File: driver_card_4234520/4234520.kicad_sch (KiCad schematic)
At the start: 30 parts, among them U1 74LS74, U10 74LS155, U11 74LS02, U12 74LS09, U13 74LS244, U14 74LS244, U15 74LS21, U16 74LS244, U17 74LS374, U18 74LS374, U19 74LS374, U2 74LS08, U20 74LS245, U21 74LS244, U22 74LS244, U23 74LS244, U24 74LS32, U3 74LS04, U4 74LS74, U5 74LS32, U6 74LS10, U7 74LS74, U8 74LS138, U9 74LS00

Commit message: Tracing finished
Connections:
- net ##4: no longer U2.4
- net ##5: now also U7.11 (C); no longer U2.11
- net 5V: now also U7.10 (~{S}), U7.12 (D)
- net GND: now also U13.1 (OEa), U16.1 (OEa), U21.1 (OEa), U21.19 (OEb), U22.1 (OEa), U22.19 (OEb), U23.1 (OEa), U23.19 (OEb)
- net ##28: now reaches U1.2 (D)
- net ##28: now also J?.51, R3.13, U14.18 (O0a), U17.2 (O0), U17.3 (D0), U18.2 (O0), U19.2 (O0), U20.2 (A0)
- net ##29: now reaches U1.3 (C)
- net ##29: now also U10.12 (Q3b)
- net ##30: now reaches U1.5 (Q)
- net ##30: now also U14.2 (I0a), U4.4 (~{S})
- net ##31: now reaches U1.6 (~{Q})
- net ##31: now also U11.3, U13.19 (OEb), U16.19 (OEb), U16.6 (I2a), U24.10, U24.2, U24.5
- net ##44: now reaches U7.13 (~{R})
- net ##44: now also U10.10 (Q1b)
- net ##46: now reaches U7.9 (Q)
- net ##46: now also U14.4 (I1a)
- net ##32: now reaches U2.2
- net ##32: now also U4.6 (~{Q})
- net ##35: now reaches U2.5
- net ##35: now also J?.3, R1.10
- net ##36: now reaches U3.2
- net ##36: now also U10.1 (Ea1)
- net ##37: now reaches U3.3
- net ##37: now also J?.2 (RESET), U24.12
- net ##50: now reaches R1.11
- net ##50: now also J?.43, U24.1
- net ##60: now reaches R1.2
- net ##60: now also J?.45, U14.17 (I3b), U16.13 (I1b)
- net ##61: now reaches R1.4
- net ##61: now also J?.49, U14.15 (I2b), U24.9
- net ##62: now reaches R1.6
- net ##62: now also J?.25, U14.11 (I0b), U24.4
- net ##51: now reaches R1.9
- net ##51: now also J?.4, U11.2, U14.6 (I2a)
- net ##38: now reaches U3.6
- net ##38: now also U5.5, U6.1
- net ##64: now reaches U10.13 (A0)
- net ##64: now also J?.13, U19.7 (D2), U22.16 (O1a)
- net ##63: now reaches U10.14 (Eb1)
- net ##63: now also U13.12 (O3a)
- net ##23: now reaches U10.15 (Eb2)
- net ##23: now also U10.2 (Ea2), U5.9, U8.10 (O5)
- net ##76: now reaches U10.3 (A1)
- net ##76: now also J?.12, U19.8 (D3), U22.5 (O2b)
- net ##77: now reaches U10.4 (Q3a)
- net ##77: now also U14.1 (OEa), U14.19 (OEb)
- net ##78: now reaches U10.5 (Q2a)
- net ##78: now also U18.1 (OE)
- net ##79: now reaches U10.6 (Q1a)
- net ##79: now also U19.1 (OE)
- net ##80: now reaches U10.7 (Q0a)
- net ##80: now also U17.1 (OE)
- net ##65: now reaches U10.9 (Q0b)
- net ##65: now also U17.11 (Cp)
- net ##43: now reaches U11.1
- net ##43: now also U6.2
- net ##39: now reaches U4.3 (C)
- net ##39: now also U16.18 (O0a)
- net ##81: now reaches U11.5
- net ##81: now also J?.15, U18.4 (D1), U21.14 (O2a)
- net ##82: now reaches U11.6
- net ##82: now also J?.41, U18.7 (D2), U21.16 (O1a)
- net ##40: now reaches U5.1
- net ##40: now also J?.29, U11.12, U23.9 (O0b), U8.5 (E2)
- net ##41: now reaches U5.3
- net ##41: now also U9.9
- net ##67: now reaches U11.8
- net ##67: now also J?.9, U18.14 (D5), U21.5 (O2b)
- net ##66: now reaches U11.9
- net ##66: now also J?.38, U18.17 (D6), U21.7 (O1b)
- net ##25: now reaches U5.4
- net ##25: now also U6.13, U9.8
- net ##42: now reaches U5.6
- net ##42: now also U6.4, U6.5
- net ##48: now reaches U11.11
- net ##48: now also U13.18 (O0a), U9.12
- net ##57: now reaches U11.13
- net ##57: now also U9.4
- net ##24: now reaches U5.8
- net ##24: now also U6.11
- net ##83: now reaches U12.2
- net ##83: now also R2.1, U16.7 (O1b)
- net ##84: now reaches U12.3
- net ##84: now also J?.41 (IO_READY), R2.5
- net ##85: now reaches U12.4
- net ##85: now also U12.5, U24.3
- net ##86: now reaches U12.6
- net ##86: now also J?.21 (IRQ7), R2.2
- net ##70: now reaches U12.10
- net ##70: now also U12.9, U24.6
- net ##71: now reaches U12.8
- net ##71: now also J?.8 (UNUSED), R2.13
- net ##26: now reaches U6.12
- net ##26: now also U6.3
- net ##69: now reaches U12.11
- net ##69: now also J?.32 (IO), R2.4
- net ##68: now reaches U12.12
- net ##68: now also U12.13, U24.8
- net ##27: now reaches U6.8
- net ##27: now also U20.1 (A->B)
- net ##75: now reaches U13.11 (I0b)
- net ##75: now also J?.11 (~{SMEMW}), U13.2 (I0a)
- net ##74: now reaches U13.13 (I1b)
- net ##74: now also J?.14 (~{IOR}), U13.4 (I1a)
- net ##47: now reaches U13.14 (O2a)
- net ##47: now also U9.10, U9.13
- net ##73: now reaches U13.15 (I2b)
- net ##73: now also J?.12 (~{SMEMR}), U13.6 (I2a)
- net ##72: now reaches U13.17 (I3b)
- net ##72: now also J?.13 (~{IOW}), U13.8 (I3a)
- net ##87: now reaches U13.3 (O3b)
- net ##87: now also J?.20, R2.12
- net ##88: now reaches U13.5 (O2b)
- net ##88: now also J?.34, R2.10
- net ##89: now reaches U13.7 (O1b)
- net ##89: now also J?.39, R2.9
- net ##90: now reaches U13.9 (O0b)
- net ##90: now also J?.35, R2.8
- net ##52: now reaches U8.1 (A0)
- net ##52: now also J?.21, U19.14 (D5), U22.7 (O1b)
- net ##53: now reaches U8.2 (A1)
- net ##53: now also J?.32, U19.13 (D4), U22.14 (O2a)
- net ##54: now reaches U8.4 (E1)
- net ##54: now also U9.3
- net ##45: now reaches U8.6 (E3)
- net ##45: now also U2.11
- net ##55: now reaches U9.1
- net ##55: now also J?.31, U19.17 (D6), U22.12 (O3a)
- net ##56: now reaches U9.2
- net ##56: now also J?.11, U19.18 (D7), U22.9 (O0b)
- net ##93: now reaches U14.12 (O3a)
- net ##93: now also J?.56, R3.10, U17.8 (D3), U17.9 (O3), U18.9 (O3), U19.9 (O3), U20.5 (A3)
- net ##92: now reaches U14.14 (O2a)
- net ##92: now also J?.52, R3.11, U17.6 (O2), U17.7 (D2), U18.6 (O2), U19.6 (O2), U20.4 (A2)
- net ##91: now reaches U14.16 (O1a)
- net ##91: now also J?.48, R3.12, U17.4 (D1), U17.5 (O1), U18.5 (O1), U19.5 (O1), U20.3 (A1)
- net ##101: now reaches U14.3 (O3b)
- net ##101: now also J?.47, R2.3, U17.18 (D7), U17.19 (O7), U18.19 (O7), U19.19 (O7), U20.9 (A7)
- net ##102: now reaches U14.5 (O2b)
- net ##102: now also J?.44, R2.6, U17.16 (O6), U17.17 (D6), U18.16 (O6), U19.16 (O6), U20.8 (A6)
- net ##103: now reaches U14.7 (O1b)
- net ##103: now also J?.22, R2.7, U17.14 (D5), U17.15 (O5), U18.15 (O5), U19.15 (O5), U20.7 (A5)
- net ##98: now reaches U14.8 (I3a)
- net ##98: now also J?.1, R2.11
- net ##104: now reaches U14.9 (O0b)
- net ##104: now also J?.53, R3.9, U17.12 (O4), U17.13 (D4), U18.12 (O4), U19.12 (O4), U20.6 (A4)
- net ##105: now reaches U15.1
- net ##105: now also J?.30, U23.12 (O3a)
- net ##106: now reaches U15.2
- net ##106: now also J?.33, U23.14 (O2a)
- net ##107: now reaches U15.4
- net ##107: now also J?.7, U23.16 (O1a)
- net ##108: now reaches U15.5
- net ##108: now also J?.8, U23.18 (O0a)
- net ##58: now reaches U15.6
- net ##58: now also U9.5
- net ##96: now reaches U15.10
- net ##96: now also J?.16, U18.8 (D3), U21.18 (O0a)
- net ##95: now reaches U15.12
- net ##95: now also J?.18, U18.13 (D4), U21.3 (O3b)
- net ##94: now reaches U15.13
- net ##94: now also J?.14, U19.4 (D1), U22.3 (O3b)
- net ##97: now reaches U15.9
- net ##97: now also J?.36, U18.3 (D0), U21.12 (O3a)
- net ##59: now reaches U9.6
- net ##59: now also U18.11 (Cp), U19.11 (Cp)
- net ##49: now reaches U9.11
- net ##49: now also U2.4
- net ##100: now reaches U16.12 (O3a)
- net ##100: now also J?.10
- net ##99: now reaches U16.14 (O2a)
- net ##99: now also J?.28
- net ##141: now reaches U16.2 (I0a)
- net ##141: now also J?.20 (CLK)
- net ##109: now reaches U16.4 (I1a)
- net ##109: now also J?.2, ZR1.6 (R3.2)
- net ##117: now reaches U20.11 (B7)
- net ##117: now also J?.33 (DB7), R3.8
- net ##116: now reaches U20.12 (B6)
- net ##116: now also J?.34 (DB6), R3.7
- net ##115: now reaches U20.13 (B5)
- net ##115: now also J?.35 (DB5), R3.6
- net ##114: now reaches U20.14 (B4)
- net ##114: now also J?.36 (DB4), R3.5
- net ##113: now reaches U20.15 (B3)
- net ##113: now also J?.37 (DB3), R3.4
- net ##112: now reaches U20.16 (B2)
- net ##112: now also J?.38 (DB2), R3.3
- net ##111: now reaches U20.17 (B1)
- net ##111: now also J?.39 (DB1), R3.2
- net ##110: now reaches U20.18 (B0)
- net ##110: now also J?.40 (DB0), R3.1
- net ##121: now reaches U21.11 (I0b)
- net ##121: now also J?.55 (BA07)
- net ##120: now reaches U21.13 (I1b)
- net ##120: now also J?.56 (BA06)
- net ##119: now reaches U21.15 (I2b)
- net ##119: now also J?.57 (BA05)
- net ##118: now reaches U21.17 (I3b)
- net ##118: now also J?.58 (BA04)
- net ##125: now reaches U21.2 (I0a)
- net ##125: now also J?.59 (BA03)
- net ##124: now reaches U21.4 (I1a)
- net ##124: now also J?.60 (BA02)
- net ##123: now reaches U21.6 (I2a)
- net ##123: now also J?.61 (BA01)
- net ##122: now reaches U21.8 (I3a)
- net ##122: now also J?.62 (BA00)
- net ##129: now reaches U22.11 (I0b)
- net ##129: now also J?.47 (BA15)
- net ##128: now reaches U22.13 (I1b)
- net ##128: now also J?.49 (BA13)
- net ##127: now reaches U22.15 (I2b)
- net ##127: now also J?.51 (BA11)
- net ##126: now reaches U22.17 (I3b)
- net ##126: now also J?.53 (BA09)
- net ##133: now reaches U22.2 (I0a)
- net ##133: now also J?.54 (BA08)
- net ##132: now reaches U22.4 (I1a)
- net ##132: now also J?.52 (BA10)
- net ##131: now reaches U22.6 (I2a)
- net ##131: now also J?.50 (BA12)
- net ##130: now reaches U22.8 (I3a)
- net ##130: now also J?.48 (BA14)
- net ##135: now reaches U23.11 (I0b)
- net ##135: now also J?.42 (AEN)
- net ##134: now reaches U23.13 (I1b)
- net ##134: now also J?.28 (ALE)
- net ##139: now reaches U23.2 (I0a)
- net ##139: now also J?.46 (BA16)
- net ##138: now reaches U23.4 (I1a)
- net ##138: now also J?.45 (BA17)
- net ##137: now reaches U23.6 (I2a)
- net ##137: now also J?.44 (BA18)
- net ##140: now reaches U23.7 (O1b)
- net ##140: now also J?.26
- net ##136: now reaches U23.8 (I3a)
- net ##136: now also J?.43 (BA19)
- no-connect marks 0 -> 54

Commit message: copy over PCB layout from earlier project add custom symbols for r networks add custom footprint for ISA XT bus add and label test point vias add filter caps missing from original schematic
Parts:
- added C1, C2, C4, C5, C6, C7, C8: 104, Capacitor_THT:C_Rect_L7.0mm_W2.0mm_P5.00mm, symbol Device:C
- added C3, C9: 106, Capacitor_THT:C_Rect_L7.0mm_W2.0mm_P5.00mm, symbol Device:C_Polarized_Small_US
- J1: renamed from J?; footprint (none) -> custom:BUS_XT
- J2: renamed from J?; footprint (none) -> Connector_Dsub:DSUB-62-HD_Female_Horizontal_P2.41x1.98mm_EdgePinOffset3.03mm_Housed_MountingHolesOffset4.94mm
- R1: footprint (none) -> Package_DIP:DIP-16_W7.62mm; symbol custom:316E221331 -> custom:R_Network_Dividers_AB_316E
- R2, R3: footprint (none) -> Package_DIP:DIP-14_W7.62mm; symbol custom:314A822 -> custom:R_Array_AB_314A
- U1, U11, U12, U15, U2, U24, U3, U4, U5, U6, U7, U9: footprint (none) -> Package_DIP:DIP-14_W7.62mm
- U10, U8: footprint (none) -> Package_DIP:DIP-16_W7.62mm
- U13, U14, U16, U17, U18, U19, U20, U21, U22, U23: footprint (none) -> Package_DIP:DIP-20_W7.62mm
- ZR1: symbol Device:R_Pack03_SIP -> custom:R_Array_AB_106B
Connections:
- net 5V: now also C1.1, C2.1, C3.1, C4.1, C5.1, C6.1, C7.1, C8.1, C9.1
- net GND: now also C1.2, C2.2, C3.2, C4.2, C5.2, C6.2, C7.2, C8.2, C9.2

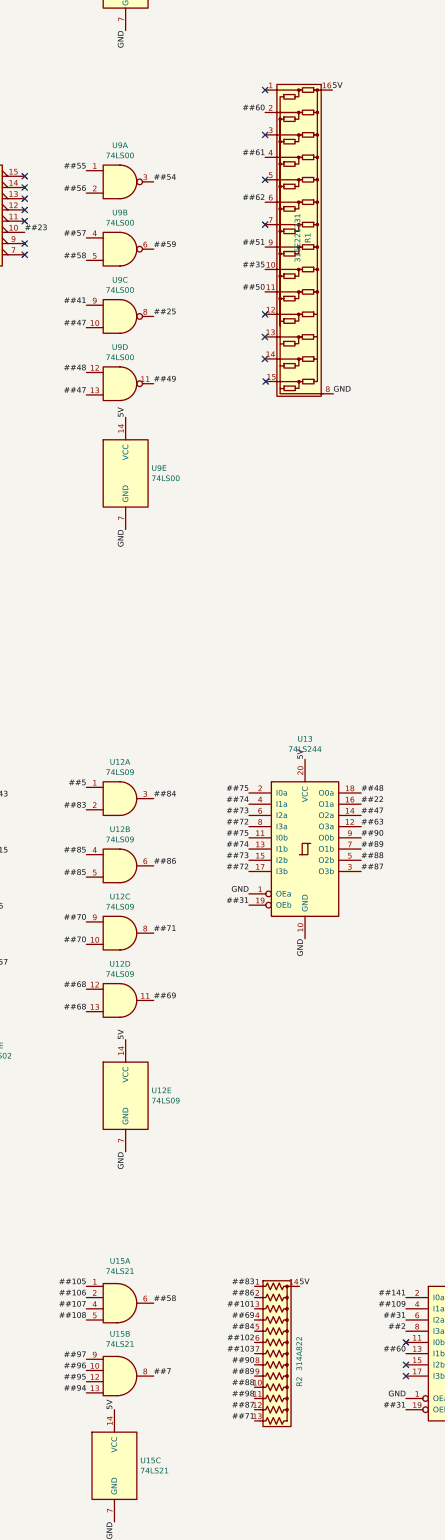
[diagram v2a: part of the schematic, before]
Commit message: make library paths relative convert to 4 layer pcb add gnd and 5v planes symbol cleanup ERC zero errors!
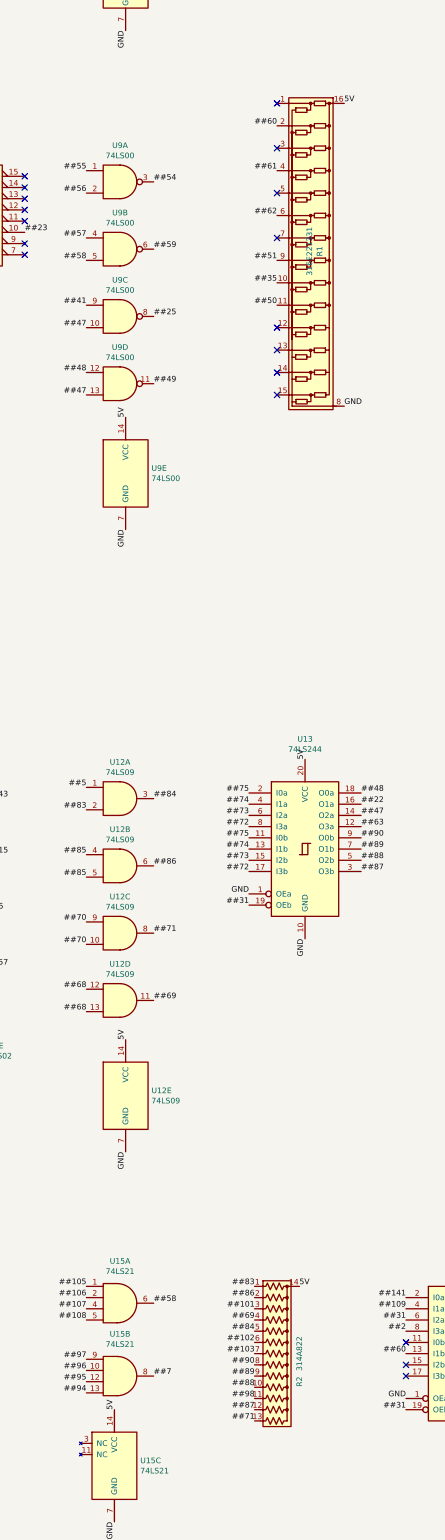
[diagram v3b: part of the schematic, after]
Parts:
- U15: symbol 74xx:74LS21 -> custom:74LS21
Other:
- moved on the sheet: R1
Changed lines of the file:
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@@
 (kicad_sch (version 20230121) (generator eeschema)
   (paper "User" 594.004 840.003)
+  (no_connect (at 153.67 151.13))
   (no_connect (at 109.22 576.58))
   (no_connect (at 96.52 170.18))
   (no_connect (at 72.39 427.99))
   (no_connect (at 297.18 670.56))
-  (no_connect (at 150.9776 158.2674))
+  (no_connect (at 153.67 161.29))
   (no_connect (at 109.22 579.12))
   (no_connect (at 35.56 167.64))
@@
   (no_connect (at 182.88 439.42))
   (no_connect (at 96.52 185.42))
-  (no_connect (at 150.9268 204.0382))
-  (no_connect (at 150.9776 178.5874))
+  (no_connect (at 153.67 207.01))
+  (no_connect (at 153.67 181.61))
   (no_connect (at 96.52 175.26))
   (no_connect (at 35.56 170.18))
-  (no_connect (at 150.9776 198.9074))
+  (no_connect (at 153.67 201.93))
   (no_connect (at 271.78 670.56))
   (no_connect (at 50.8 167.64))
   (no_connect (at 72.39 420.37))
-  (no_connect (at 150.9268 209.0166))
+  (no_connect (at 153.67 212.09))
   (no_connect (at 208.28 436.88))
   (no_connect (at 72.39 422.91))
@@
   (no_connect (at 96.52 177.8))
   (no_connect (at 317.5 670.56))
-  (no_connect (at 151.13 214.122))
+  (no_connect (at 153.67 217.17))
   (no_connect (at 43.18 177.8))
   (no_connect (at 50.8 172.72))
@@
   (no_connect (at 165.1 40.64))
   (no_connect (at 96.52 182.88))
-  (no_connect (at 150.9776 148.1074))
   (no_connect (at 294.64 670.56))
   (no_connect (at 182.88 436.88))
@@
   (no_connect (at 266.7 670.56))
   (no_connect (at 58.42 325.12))
-  (no_connect (at 150.9776 168.4274))
+  (no_connect (at 153.67 171.45))
   (no_connect (at 182.88 431.8))
   (label "##135" (at 307.34 706.12 270) (fields_autoplaced)
@@
     (effects (font (size 1.27 1.27)) (justify left bottom))
   )
-  (label "5V" (at 166.2176 148.1074 0) (fields_autoplaced)
+  (label "5V" (at 168.91 151.13 0) (fields_autoplaced)
     (effects (font (size 1.27 1.27)) (justify left bottom))
   )
@@
     (effects (font (size 1.27 1.27)) (justify right bottom))
   )
-  (label "##51" (at 150.9776 183.6674 180) (fields_autoplaced)
+  (label "##51" (at 153.67 186.69 180) (fields_autoplaced)
     (effects (font (size 1.27 1.27)) (justify right bottom))
   )
@@
     (effects (font (size 1.27 1.27)) (justify right bottom))
   )
-  (label "GND" (at 166.4462 216.916 0) (fields_autoplaced)
+  (label "GND" (at 168.91 219.71 0) (fields_autoplaced)
     (effects (font (size 1.27 1.27)) (justify left bottom))
   )
@@
     (effects (font (size 1.27 1.27)) (justify right bottom))
   )
-  (label "##60" (at 150.9776 153.1874 180) (fields_autoplaced)
+  (label "##60" (at 153.67 156.21 180) (fields_autoplaced)
     (effects (font (size 1.27 1.27)) (justify right bottom))
   )
@@
     (effects (font (size 1.27 1.27)) (justify right bottom))
   )
-  (label "##50" (at 150.9776 193.8274 180) (fields_autoplaced)
+  (label "##50" (at 153.67 196.85 180) (fields_autoplaced)
     (effects (font (size 1.27 1.27)) (justify right bottom))
   )
@@
     (effects (font (size 1.27 1.27)) (justify left bottom))
   )
-  (label "##62" (at 150.9776 173.5074 180) (fields_autoplaced)
+  (label "##62" (at 153.67 176.53 180) (fields_autoplaced)
     (effects (font (size 1.27 1.27)) (justify right bottom))
   )
@@
     (effects (font (size 1.27 1.27)) (justify right bottom))
   )
-  (label "##35" (at 150.9776 188.7474 180) (fields_autoplaced)
+  (label "##35" (at 153.67 191.77 180) (fields_autoplaced)
     (effects (font (size 1.27 1.27)) (justify right bottom))
   )
@@
     (effects (font (size 1.27 1.27)) (justify right bottom))
   )
-  (label "##61" (at 150.9776 163.3474 180) (fields_autoplaced)
+  (label "##61" (at 153.67 166.37 180) (fields_autoplaced)
     (effects (font (size 1.27 1.27)) (justify right bottom))
   )
@@
   (symbol (lib_id "custom:R_Network_Dividers_AB_316E") (at 158.75 181.61 270) (unit 1)
     (in_bom yes) (on_board yes) (dnp no)
-    (property "Reference" "R1" (at 160.655 181.61 0)
+    (property "Reference" "R1" (at 163.3474 184.6326 0)
       (effects (font (size 1.27 1.27)))
     )
-    (property "Value" "316E221331" (at 158.3436 181.61 0)
+    (property "Value" "316E221331" (at 161.036 184.6326 0)
       (effects (font (size 1.27 1.27)))
     )
-    (property "Footprint" "Package_DIP:DIP-16_W7.62mm" (at 158.7246 222.1484 90)
+    (property "Footprint" "Package_DIP:DIP-16_W7.62mm" (at 161.417 225.171 90)
       (effects (font (size 1.27 1.27)) hide)
     )
-    (property "Datasheet" "" (at 158.5976 173.5074 0)
+    (property "Datasheet" "" (at 161.29 176.53 0)
       (effects (font (size 1.27 1.27)) hide)
     )
@@
     )
   )
-  (symbol (lib_id "74xx:74LS21") (at 116.84 459.74 0) (unit 3)
+  (symbol (lib_id "custom:74LS21") (at 116.84 459.74 0) (unit 3)
     (in_bom yes) (on_board yes) (dnp no)
     (property "Reference" "U15" (at 122.682 458.5716 0)
@@
     (pin "14")
     (pin "7")
+    (pin "11")
+    (pin "3")
     (instances
       (project "4234520"

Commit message: Add redrawn schematic, courtesy of Tube Time (@schlae)
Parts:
- removed C1, C2, C4, C5, C6, C7, C8: 104, Capacitor_THT:C_Rect_L7.0mm_W2.0mm_P5.00mm, symbol Device:C
- removed C3, C9: 106, Capacitor_THT:C_Rect_L7.0mm_W2.0mm_P5.00mm, symbol Device:C_Polarized_Small_US
- J?: renamed from J1; footprint custom:BUS_XT -> (none)
- J?: renamed from J2; footprint Connector_Dsub:DSUB-62-HD_Female_Horizontal_P2.41x1.98mm_EdgePinOffset3.03mm_Housed_MountingHolesOffset4.94mm -> (none)
- R1: footprint Package_DIP:DIP-16_W7.62mm -> (none); symbol custom:R_Network_Dividers_AB_316E -> custom:316E221331
- R2, R3: footprint Package_DIP:DIP-14_W7.62mm -> (none); symbol custom:R_Array_AB_314A -> custom:314A822
- U1, U11, U12, U15, U2, U24, U3, U4, U5, U6, U7, U9: footprint Package_DIP:DIP-14_W7.62mm -> (none)
- U10, U8: footprint Package_DIP:DIP-16_W7.62mm -> (none)
- U13, U14, U16, U17, U18, U19, U20, U21, U22, U23: footprint Package_DIP:DIP-20_W7.62mm -> (none)
- U15: footprint Package_DIP:DIP-14_W7.62mm -> (none); symbol custom:74LS21 -> 74xx:74LS21
- ZR1: symbol custom:R_Array_AB_106B -> Device:R_Pack03_SIP
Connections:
- net ##100 renamed ~{REFRESH}_B
- net ##101 renamed ADB7
- net ##102 renamed ADB6
- net ##103 renamed ADB5
- net ##104 renamed ADB4
- net ##105 renamed AA19
- net ##106 renamed AA18
- net ##107 renamed AA17
- net ##108 renamed AA16
- net ##109 renamed ~{EXT_RESET}
- net ##11 renamed ~{EXT_RESET}_B
- net ##110 renamed DB0
- net ##111 renamed DB1
- net ##112 renamed DB2
- net ##113 renamed DB3
- net ##114 renamed DB4
- net ##115 renamed DB5
- net ##116 renamed DB6
- net ##117 renamed DB7
- net ##118 renamed A4
- net ##119 renamed A5
- net ##120 renamed A6
- net ##121 renamed A7
- net ##122 renamed A0
- net ##123 renamed A1
- net ##124 renamed A2
- net ##125 renamed A3
- net ##126 renamed A9
- net ##127 renamed A11
- net ##128 renamed A13
- net ##129 renamed A15
- net ##130 renamed A14
- net ##131 renamed A12
- net ##132 renamed A10
- net ##133 renamed A8
- net ##134 renamed ALE
- net ##135 renamed AEN
- net ##136 renamed A19
- net ##137 renamed A18
- net ##138 renamed A17
- net ##139 renamed A16
- net ##140 renamed ALE_B
- net ##141 renamed CLK
- net ##17 renamed ~{DBUF_OE}
- net ##18 renamed ~{RESET}
- net ##2 renamed ~{REFRESH}
- net ##20 renamed AA8
- net ##21 renamed AA7
- net ##22 renamed ~{IOR}_B1
- net ##23 renamed ~{CARD_SEL}
- net ##27 renamed READ_DIR
- net ##28 renamed ADB0
- net ##29 renamed ~{CARD_EN_REG}
- net ##30 renamed CARD_EN
- net ##31 renamed ~{CARD_EN}
- net ##35 renamed DO_WAIT_STATE
- net ##36 renamed IOR_B1
- net ##37 renamed RESET
- net ##39 renamed CLK_B
- net ##40 renamed AEN_B
- net ##44 renamed ~{CLR_UNK_FLAG}
- net ##46 renamed UNK_FLAG
- net ##47 renamed ~{MEMR}_B1
- net ##48 renamed ~{MEMW}_B1
- net ##50 renamed ~{EXT_IRQ}
- net ##51 renamed UNK_STATUS1
- net ##52 renamed AA13
- net ##53 renamed AA12
- net ##55 renamed AA14
- net ##56 renamed AA15
- net ##59 renamed CAPTURE_ADDR16
- net ##60 renamed EN_WAIT_STATE
- net ##61 renamed ~{EXT_IOERR}
- net ##62 renamed ~{EXT_0WAIT}
- net ##63 renamed ~{IOW}_B1
- net ##64 renamed AA10
- net ##65 renamed ~{LOOPBACK_WR}
- net ##66 renamed AA6
- net ##67 renamed AA5
- net ##69 renamed ~{IOERR}
- net ##71 renamed ~{ZERO_WAIT}
- net ##72 renamed ~{IOW}
- net ##73 renamed ~{MEMR}
- net ##74 renamed ~{IOR}
- net ##75 renamed ~{MEMW}
- net ##76 renamed AA11
- net ##77 renamed ~{STATUS_RD}
- net ##78 renamed ~{READBACK_ADDRL}
- net ##79 renamed ~{READBACK_ADDRH}
- net ##80 renamed ~{LOOPBACK_RD}
- net ##81 renamed AA1
- net ##82 renamed AA2
- net ##83 renamed EN_WAIT_STATE_B
- net ##84 renamed IORDY
- net ##86 renamed ~{IRQ7}
- net ##87 renamed ~{IOW}_B2
- net ##88 renamed ~{MEMR}_B2
- net ##89 renamed ~{IOR}_B2
- net ##90 renamed ~{MEMW}_B2
- net ##91 renamed ADB1
- net ##92 renamed ADB2
- net ##93 renamed ADB3
- net ##94 renamed AA9
- net ##95 renamed AA4
- net ##96 renamed AA3
- net ##97 renamed AA0
- net ##98 renamed UNK_STATUS2
- net ##99 renamed ~{CARD_EN}_B
- net 5V renamed +5V
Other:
- note added: "0"
- note added: "1"
- note added: "ADDRESS BUFFERS"
- note added: "ADDRESS DECODER"
- note added: "CARD ENABLE REGISTER"
- note added: "DATA BUFFER CONTROL"
- note added: "E219"
- note added: "E619"
- note added: "EA19"
- note added: "EE19"
- note added: "IO Address = 1110 xx10 0001 1001 = Ex19"
- note added: "IRQ, IOERR, ZERO WAIT"
- note added: "LATCH 16 ADDRESS BITS FOR LOOPBACK TEST"
- note added: "LOOPBACK TEST REGISTER"
- note added: "MISC BUFFER"
- note added: "Memory write Fxxxx:xxxx"
- note added: "POWER CONNECTIONS"
- note added: "PULLUPS"
- note added: "REGISTER SELECT"
- note added: "STATUS REGISTER"
- note added: "WAIT STATE MACHINE"
- moved on the sheet: J?, U10, U11A, U11B, U11C, U11D, U11E, U12A, U12B, U12C, U12D, U12E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

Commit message: update tubetime's sch for r-pack symbols, clean up DRC
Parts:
- R1: footprint (none) -> Package_DIP:DIP-16_W7.62mm; symbol custom:316E221331 -> custom:R_Network_Dividers_AB_316E
- R2, R3: footprint (none) -> Package_DIP:DIP-14_W7.62mm; symbol custom:314A822 -> custom:R_Array_AB_314A
- gave numbers to parts that had none: 2
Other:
- moved on the sheet: U16, U7A, ZR1
